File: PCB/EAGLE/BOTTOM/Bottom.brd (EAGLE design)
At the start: 100 x 35 mm, 81 parts, among them J1 \, J2 Anodes, J3 2X6 FEMALE, Q1 MMBTA42, Q10 MMBTA92, Q11 32.768, Q2 MMBTA42, Q3 MMBTA42, Q4 MMBTA42, Q5 MMBTA42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

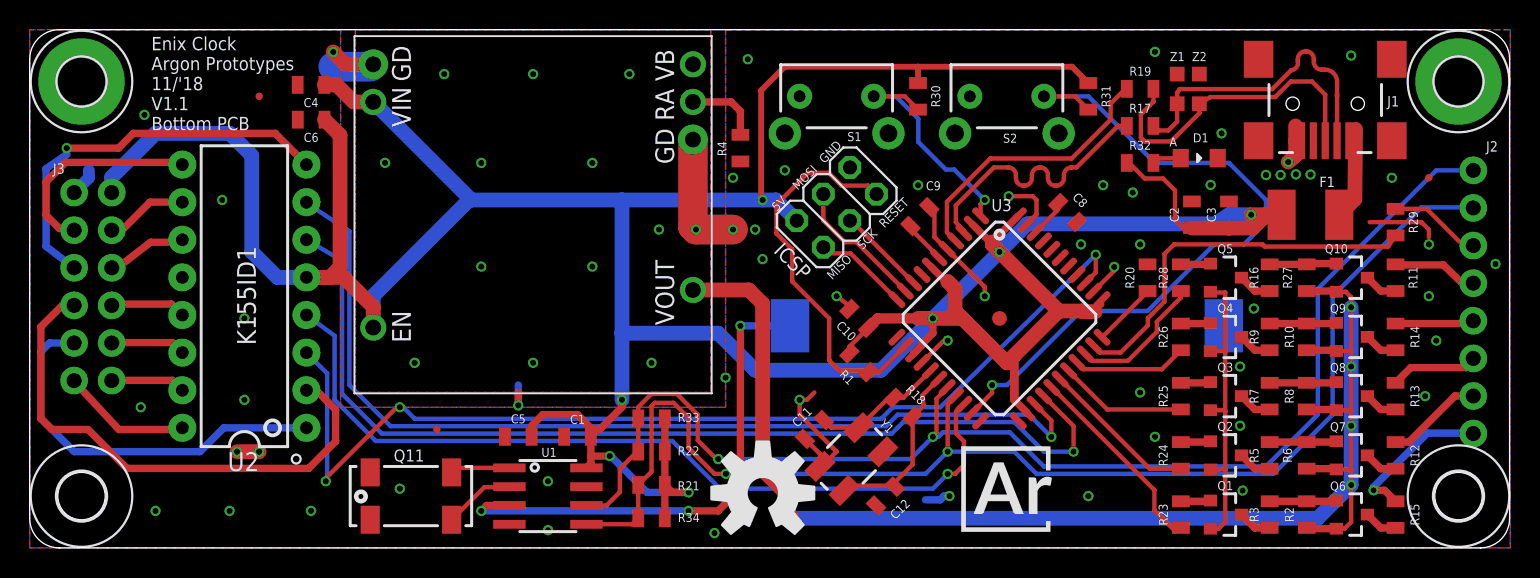
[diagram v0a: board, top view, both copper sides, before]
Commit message: Update boards to latest, update packaging photos, add 3D printed part files
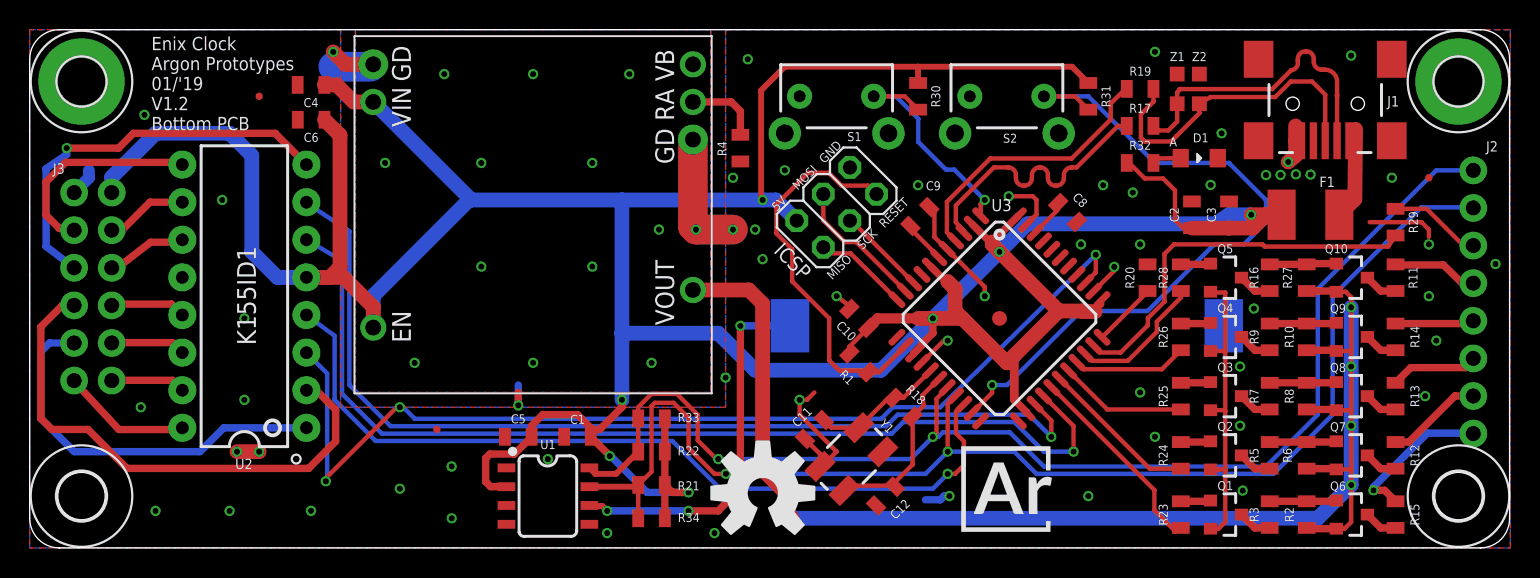
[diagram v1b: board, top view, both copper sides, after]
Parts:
- removed Q11: 32.768, microbuilder:CRYSTAL_8X3.8
- C11, C12: value 22p -> 14pF
- U1: value DS1307 -> DS3231M; device microbuilder:SOIC8_150MIL -> SparkFun-Clocks:SO08
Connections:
- removed net XI: Q11.P$1, U1.1
- removed net XO: Q11.P$4, U1.2
- net +5V: now also U1.2; no longer U1.8
- net GND: now also U1.5; no longer U1.4
- net SCL: now also U1.8; no longer U1.6
- net SDA: now also U1.7; no longer U1.5
- net SQW: now also U1.3; no longer U1.7
- net VBAT: now also U1.6; no longer U1.3
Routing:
- net VBAT: track 34.5 -> 25.3 mm
- net +5V: track 270.3 -> 275.5 mm
- net XO: track 4.83 -> 0.00 mm
- net XI: track 4.03 -> 0.00 mm
- net SCL: track 87.2 -> 85.4 mm
- net GND: vias 71 -> 73
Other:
- board text added: "Enix Clock Argon Prototypes 01/'19 V1.2 Bottom PCB"
- board text removed: "Enix Clock Argon Prototypes 11/'18 V1.1 Bottom PCB"
